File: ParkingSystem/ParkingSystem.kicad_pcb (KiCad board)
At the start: 2 copper layers, 55.9 x 61.5 mm, 43 parts, among them J1 PJ-002A, J2 0430450400, J3 Conn_ARM_JTAG_SWD_10, J4 Conn_01x04_Female, J5 0430450200, Q1 SSM3K333R,LF, Q2 SSM3K333R,LF, Q3 SSM3K333R,LF, Q4 SSM3K333R,LF, Q5 SSM3K333R,LF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

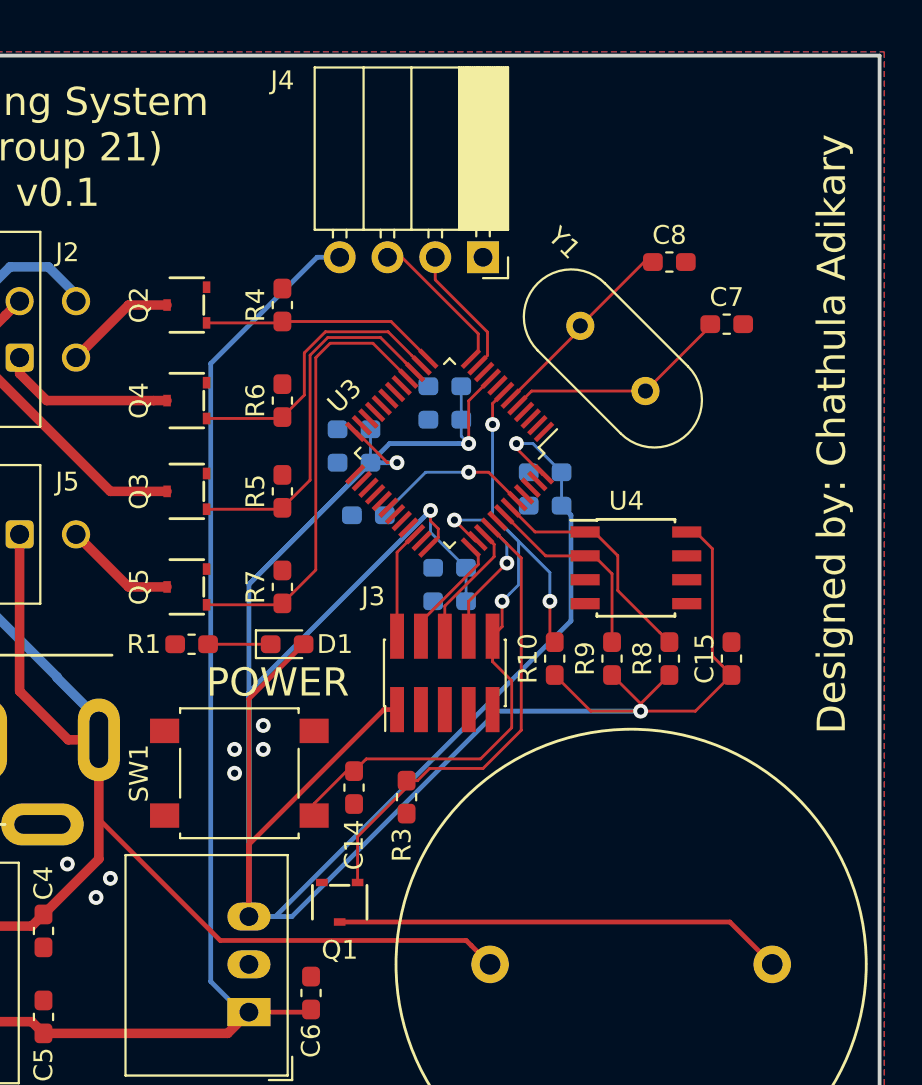
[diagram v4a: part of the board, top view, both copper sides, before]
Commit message: Add Ground Pours
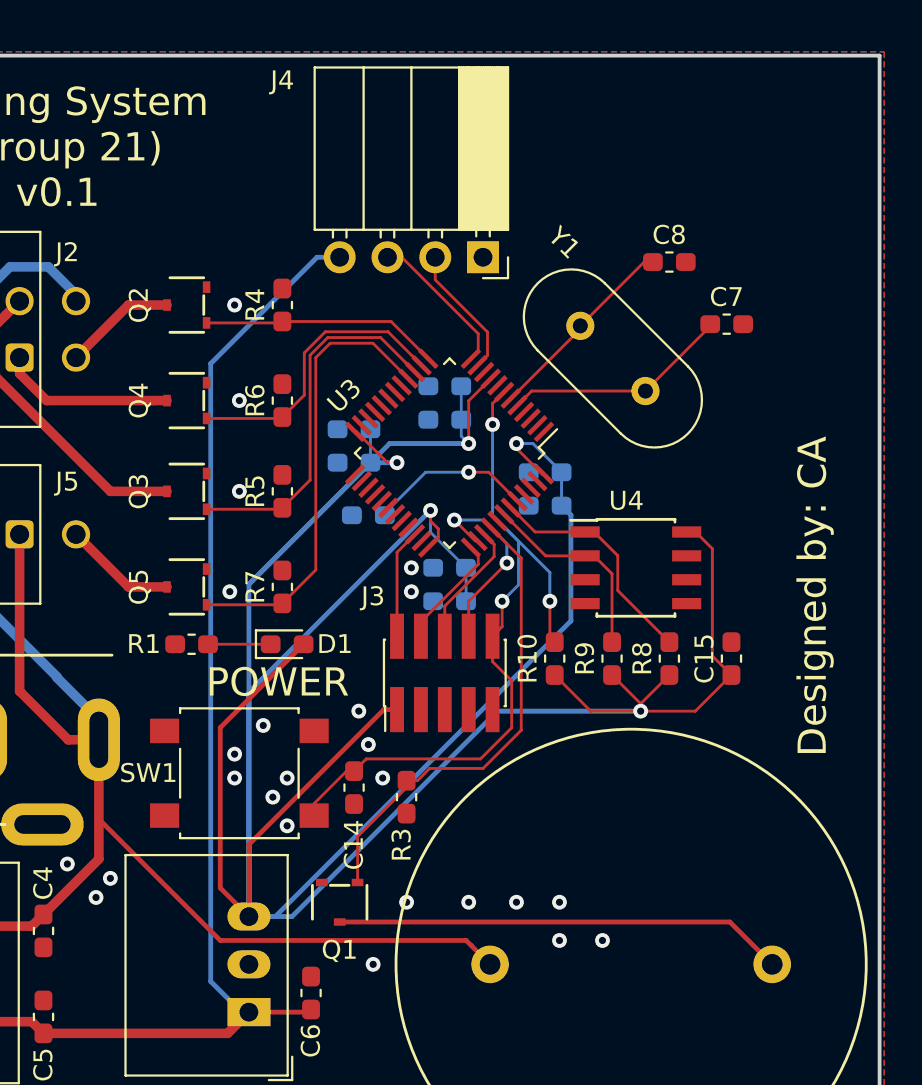
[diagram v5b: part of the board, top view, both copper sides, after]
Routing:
- net +3V3: track 205.7 -> 207.0 mm
- net GND: vias 7 -> 25
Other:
- board text added: "Designed by: CA"
- board text removed: "Designed by: Chathula Adikary"
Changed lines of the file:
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@@
     (thickness 1.6)
     (drawings 7)
-    (tracks 230)
+    (tracks 249)
     (zones 0)
     (modules 43)
@@
     (tags "capacitor handsolder")
     (attr smd)
-    (fp_text reference C2 (at 2.54 0 180) (layer B.SilkS)
+    (fp_text reference C2 (at 0 -1.524 180) (layer B.SilkS)
       (effects (font (size 1 1) (thickness 0.15)) (justify mirror))
     )
@@
     (tags "capacitor handsolder")
     (attr smd)
-    (fp_text reference C9 (at 2.54 0 180) (layer B.SilkS)
+    (fp_text reference C9 (at 0 1.27 180) (layer B.SilkS)
       (effects (font (size 1 1) (thickness 0.15)) (justify mirror))
     )
@@
     (tags "Tactile Switch")
     (attr smd)
-    (fp_text reference SW1 (at 5.334 0 270) (layer F.SilkS)
+    (fp_text reference SW1 (at 4.826 0) (layer F.SilkS)
       (effects (font (size 1 1) (thickness 0.15)))
     )
@@
     )
   )
-  (gr_text "Designed by: Chathula Adikary" (at 121.92 55.118 90) (layer F.SilkS)
+  (gr_text "Designed by: CA" (at 120.904 63.754 90) (layer F.SilkS)
     (effects (font (size 1.5 1.5) (thickness 0.3)))
   )
@@
     (effects (font (size 1.5 1.5) (thickness 0.3)))
   )
+  (via (at 99.568 62.23) (size 0.7874) (drill 0.381) (layers F.Cu B.Cu) (net 2))
+  (via (at 99.568 63.5) (size 0.7874) (drill 0.381) (layers F.Cu B.Cu) (net 2))
+  (via (at 97.282 71.628) (size 0.7874) (drill 0.381) (layers F.Cu B.Cu) (net 2))
   (via (at 106.934 64.008) (size 0.7874) (drill 0.381) (layers F.Cu B.Cu) (net 7))
   (via (at 102.616 57.15) (size 0.7874) (drill 0.381) (layers F.Cu B.Cu) (net 27))
@@
   (segment (start 90.932 76.941078) (end 98.105078 69.768) (width 0.254) (layer F.Cu) (net 1))
   (segment (start 90.932 80.772) (end 90.932 76.941078) (width 0.254) (layer F.Cu) (net 1))
-  (segment (start 90.932 69.201) (end 90.932 80.772) (width 0.254) (layer F.Cu) (net 1))
-  (segment (start 93.839 66.294) (end 90.932 69.201) (width 0.254) (layer F.Cu) (net 1))
   (segment (start 90.932 68.834) (end 100.584 59.182) (width 0.254) (layer B.Cu) (net 1))
   (segment (start 90.932 80.772) (end 90.932 68.834) (width 0.254) (layer B.Cu) (net 1))
@@
   (segment (start 114.667 69.85) (end 116.586 67.931) (width 0.1524) (layer F.Cu) (net 1))
   (segment (start 111.76 69.85) (end 114.667 69.85) (width 0.1524) (layer F.Cu) (net 1))
+  (segment (start 89.408 79.248) (end 90.932 80.772) (width 0.254) (layer F.Cu) (net 1))
+  (segment (start 93.839 66.294) (end 89.408 70.725) (width 0.254) (layer F.Cu) (net 1))
+  (segment (start 89.408 70.725) (end 89.408 79.248) (width 0.254) (layer F.Cu) (net 1))
   (via (at 82.804 79.756) (size 0.7874) (drill 0.381) (layers F.Cu B.Cu) (net 2))
   (via (at 83.566 78.74) (size 0.7874) (drill 0.381) (layers F.Cu B.Cu) (net 2))
   (via (at 81.28 77.978) (size 0.7874) (drill 0.381) (layers F.Cu B.Cu) (net 2))
   (via (at 91.694 70.612) (size 0.7874) (drill 0.381) (layers F.Cu B.Cu) (net 2))
-  (via (at 91.694 71.882) (size 0.7874) (drill 0.381) (layers F.Cu B.Cu) (net 2))
-  (via (at 90.17 71.882) (size 0.7874) (drill 0.381) (layers F.Cu B.Cu) (net 2))
-  (via (at 90.17 73.152) (size 0.7874) (drill 0.381) (layers F.Cu B.Cu) (net 2))
+  (via (at 92.202 74.422) (size 0.7874) (drill 0.381) (layers F.Cu B.Cu) (net 2))
+  (via (at 90.17 72.136) (size 0.7874) (drill 0.381) (layers F.Cu B.Cu) (net 2))
+  (via (at 92.964 75.946) (size 0.7874) (drill 0.381) (layers F.Cu B.Cu) (net 2))
+  (via (at 98.044 73.406) (size 0.7874) (drill 0.381) (layers F.Cu B.Cu) (net 2))
+  (via (at 90.17 48.26) (size 0.7874) (drill 0.381) (layers F.Cu B.Cu) (net 2))
+  (via (at 90.424 53.34) (size 0.7874) (drill 0.381) (layers F.Cu B.Cu) (net 2))
+  (via (at 90.424 58.166) (size 0.7874) (drill 0.381) (layers F.Cu B.Cu) (net 2))
+  (via (at 89.916 63.5) (size 0.7874) (drill 0.381) (layers F.Cu B.Cu) (net 2))
+  (via (at 92.964 73.406) (size 0.7874) (drill 0.381) (layers F.Cu B.Cu) (net 2))
+  (via (at 96.774 69.85) (size 0.7874) (drill 0.381) (layers F.Cu B.Cu) (net 2))
+  (via (at 90.17 73.406) (size 0.7874) (drill 0.381) (layers F.Cu B.Cu) (net 2))
+  (via (at 102.616 80.01) (size 0.7874) (drill 0.381) (layers F.Cu B.Cu) (net 2))
+  (via (at 105.156 80.01) (size 0.7874) (drill 0.381) (layers F.Cu B.Cu) (net 2))
+  (via (at 107.442 80.01) (size 0.7874) (drill 0.381) (layers F.Cu B.Cu) (net 2))
+  (via (at 107.442 82.042) (size 0.7874) (drill 0.381) (layers F.Cu B.Cu) (net 2))
+  (via (at 109.728 82.042) (size 0.7874) (drill 0.381) (layers F.Cu B.Cu) (net 2))
+  (via (at 99.314 80.01) (size 0.7874) (drill 0.381) (layers F.Cu B.Cu) (net 2))
+  (via (at 97.536 83.312) (size 0.7874) (drill 0.381) (layers F.Cu B.Cu) (net 2))
   (segment (start 81.326 71.374) (end 82.954 71.374) (width 0.508) (layer F.Cu) (net 3))
   (segment (start 78.74 68.788) (end 81.326 71.374) (width 0.508) (layer F.Cu) (net 3))
@@
     (connect_pads (clearance 0.1778))
     (min_thickness 0.1778)
-    (fill yes (arc_segments 16) (thermal_gap 0.508) (thermal_bridge_width 0.508))
+    (fill (arc_segments 16) (thermal_gap 0.508) (thermal_bridge_width 0.508))
     (polygon
       (pts
@@
     (connect_pads (clearance 0.1778))
     (min_thickness 0.1778)
-    (fill yes (arc_segments 16) (thermal_gap 0.508) (thermal_bridge_width 0.508))
+    (fill (arc_segments 16) (thermal_gap 0.508) (thermal_bridge_width 0.508))
     (polygon
       (pts

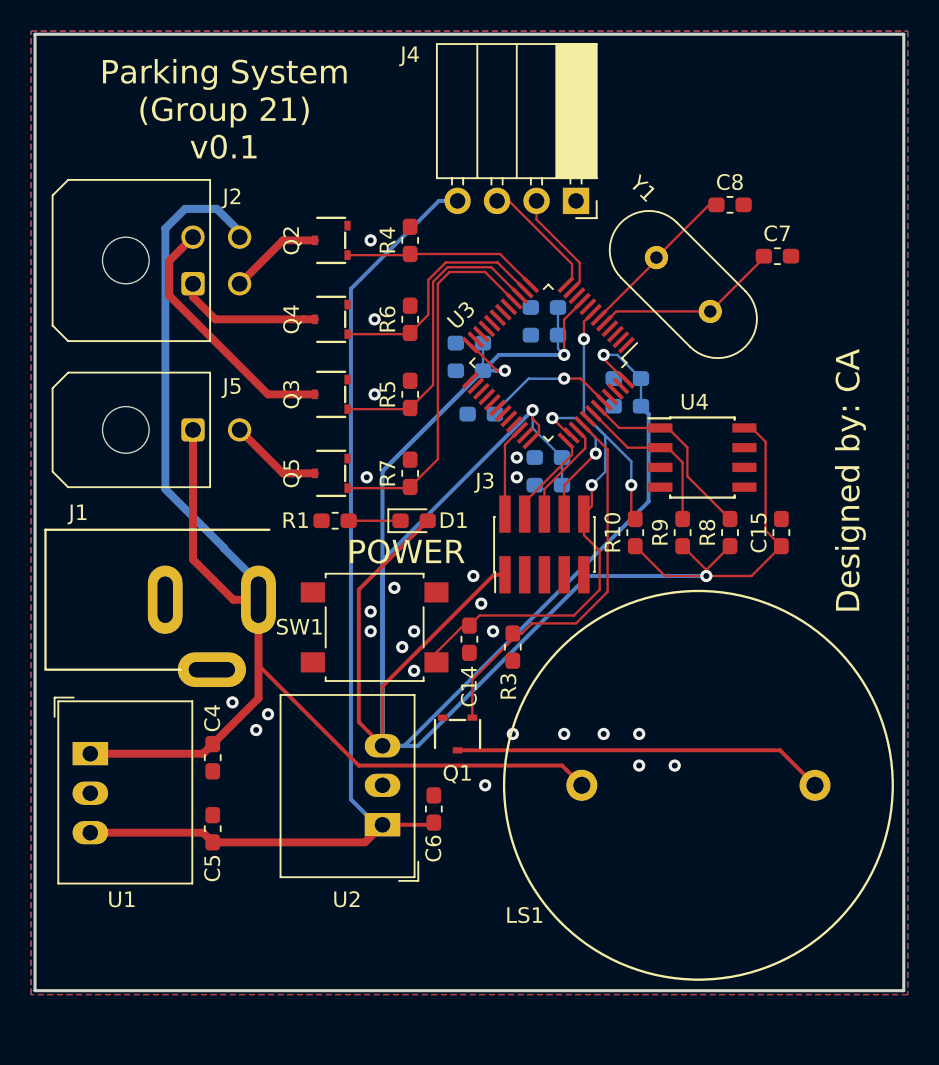
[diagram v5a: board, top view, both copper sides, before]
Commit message: Add Mounting Holes
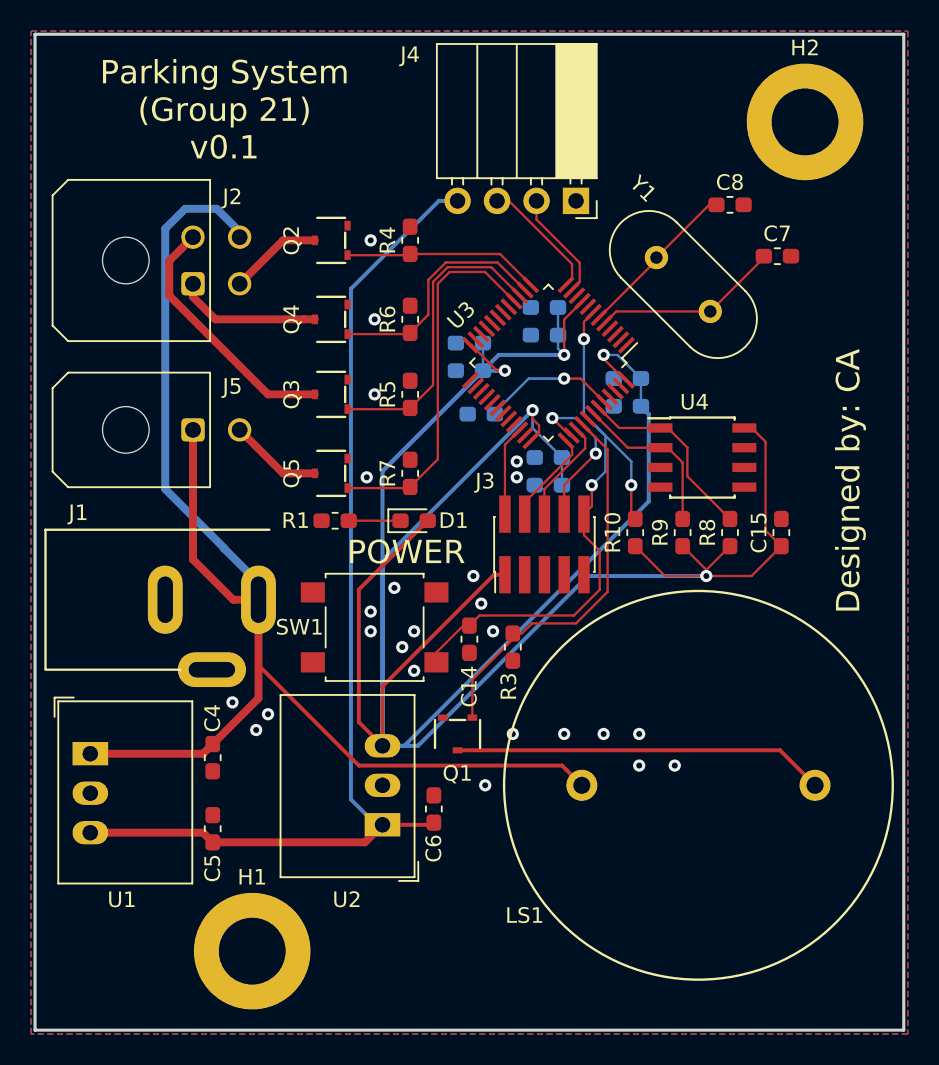
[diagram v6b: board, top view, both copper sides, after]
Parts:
- added H1: MountingHole, MountingHole:MountingHole_4.3mm_M4_DIN965_Pad, F.Cu at (82.5, 94.0)
- added H2: MountingHole, MountingHole:MountingHole_4.3mm_M4_DIN965_Pad, F.Cu at (118.1, 40.6)
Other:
- board size 55.9 x 61.5 mm -> 55.9 x 64.1 mm
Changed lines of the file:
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@@
-(kicad_pcb (version 20171130) (host pcbnew "(5.0.2)-1")
+(kicad_pcb (version 20171130) (host pcbnew 5.0.2-bee76a0~70~ubuntu18.04.1)
   (general
     (thickness 1.6)
@@
     (tracks 249)
     (zones 0)
-    (modules 43)
+    (modules 45)
     (nets 54)
   )
@@
   )
   (setup
-    (last_trace_width 0.1524)
+    (last_trace_width 0.254)
     (user_trace_width 0.1524)
     (user_trace_width 0.508)
@@
     (add_net "Net-(U4-Pad3)")
   )
+  (module MountingHole:MountingHole_4.3mm_M4_DIN965_Pad (layer F.Cu)
+    (at 118.11 40.64)
+    (descr "Mounting Hole 4.3mm, M4, DIN965")
+    (tags "mounting hole 4.3mm m4 din965")
+    (attr virtual)
+    (fp_text reference H2 (at 0 -4.75) (layer F.SilkS)
+      (effects (font (size 1 1) (thickness 0.15)))
+    )
+    (fp_text value MountingHole (at 0 4.75) (layer F.Fab)
+      (effects (font (size 1 1) (thickness 0.15)))
+    )
+    (fp_circle (center 0 0) (end 4 0) (layer F.CrtYd) (width 0.05))
+    (fp_circle (center 0 0) (end 3.75 0) (layer Cmts.User) (width 0.15))
+    (fp_text user %R (at 0.3 0) (layer F.Fab)
+      (effects (font (size 1 1) (thickness 0.15)))
+    )
+    (pad 1 thru_hole circle (at 0 0) (size 7.5 7.5) (drill 4.3) (layers *.Cu *.Mask))
+  )
+  (module MountingHole:MountingHole_4.3mm_M4_DIN965_Pad (layer F.Cu)
+    (at 82.55 93.98)
+    (descr "Mounting Hole 4.3mm, M4, DIN965")
+    (tags "mounting hole 4.3mm m4 din965")
+    (attr virtual)
+    (fp_text reference H1 (at 0 -4.75) (layer F.SilkS)
+      (effects (font (size 1 1) (thickness 0.15)))
+    )
+    (fp_text value MountingHole (at 0 4.75) (layer F.Fab)
+      (effects (font (size 1 1) (thickness 0.15)))
+    )
+    (fp_text user %R (at 0.3 0) (layer F.Fab)
+      (effects (font (size 1 1) (thickness 0.15)))
+    )
+    (fp_circle (center 0 0) (end 3.75 0) (layer Cmts.User) (width 0.15))
+    (fp_circle (center 0 0) (end 4 0) (layer F.CrtYd) (width 0.05))
+    (pad 1 thru_hole circle (at 0 0) (size 7.5 7.5) (drill 4.3) (layers *.Cu *.Mask))
+  )
   (module Converter_DCDC:Converter_DCDC_RECOM_R-78E-0.5_THT (layer F.Cu)
     (at 72.136 81.28 270)
@@
     (effects (font (size 1.5 1.5) (thickness 0.3)))
   )
-  (gr_line (start 124.46 96.52) (end 68.58 96.52) (layer Edge.Cuts) (width 0.2))
-  (gr_line (start 124.46 35) (end 124.46 96.52) (layer Edge.Cuts) (width 0.2))
+  (gr_line (start 124.46 99.06) (end 68.58 99.06) (layer Edge.Cuts) (width 0.2))
+  (gr_line (start 124.46 35) (end 124.46 99.06) (layer Edge.Cuts) (width 0.2))
   (gr_line (start 68.58 35) (end 124.46 35) (layer Edge.Cuts) (width 0.2))
-  (gr_line (start 68.58 96.52) (end 68.58 35) (layer Edge.Cuts) (width 0.2))
+  (gr_line (start 68.58 99.06) (end 68.58 35) (layer Edge.Cuts) (width 0.2))
   (gr_text POWER (at 92.456 68.326) (layer F.SilkS)
     (effects (font (size 1.5 1.5) (thickness 0.3)))
   )
-  (via (at 99.568 62.23) (size 0.7874) (drill 0.381) (layers F.Cu B.Cu) (net 2))
-  (via (at 99.568 63.5) (size 0.7874) (drill 0.381) (layers F.Cu B.Cu) (net 2))
-  (via (at 97.282 71.628) (size 0.7874) (drill 0.381) (layers F.Cu B.Cu) (net 2))
-  (via (at 106.934 64.008) (size 0.7874) (drill 0.381) (layers F.Cu B.Cu) (net 7))
-  (via (at 102.616 57.15) (size 0.7874) (drill 0.381) (layers F.Cu B.Cu) (net 27))
   (via (at 111.76 69.85) (size 0.7874) (drill 0.381) (layers F.Cu B.Cu) (net 1))
-  (via (at 101.854 59.69) (size 0.7874) (drill 0.381) (layers F.Cu B.Cu) (net 17))
   (via (at 100.584 59.182) (size 0.7874) (drill 0.381) (layers F.Cu B.Cu) (net 1))
   (via (at 98.806 56.642) (size 0.7874) (drill 0.381) (layers F.Cu B.Cu) (net 1))
-  (via (at 104.394 64.008) (size 0.7874) (drill 0.381) (layers F.Cu B.Cu) (net 7))
   (via (at 102.616 55.626) (size 0.7874) (drill 0.381) (layers F.Cu B.Cu) (net 1))
   (segment (start 97.395 56.642) (end 97.395 54.864) (width 0.1524) (layer B.Cu) (net 1))
@@
   (segment (start 93.839 66.294) (end 89.408 70.725) (width 0.254) (layer F.Cu) (net 1))
   (segment (start 89.408 70.725) (end 89.408 79.248) (width 0.254) (layer F.Cu) (net 1))
+  (via (at 99.568 62.484) (size 0.7874) (drill 0.381) (layers F.Cu B.Cu) (net 2))
+  (via (at 99.568 63.5) (size 0.7874) (drill 0.381) (layers F.Cu B.Cu) (net 2))
+  (via (at 97.282 71.628) (size 0.7874) (drill 0.381) (layers F.Cu B.Cu) (net 2))
   (via (at 82.804 79.756) (size 0.7874) (drill 0.381) (layers F.Cu B.Cu) (net 2))
   (via (at 83.566 78.74) (size 0.7874) (drill 0.381) (layers F.Cu B.Cu) (net 2))
@@
   (segment (start 111.942354 45.974) (end 112.409 45.974) (width 0.1524) (layer F.Cu) (net 6))
   (segment (start 108.549177 49.367177) (end 111.942354 45.974) (width 0.1524) (layer F.Cu) (net 6))
+  (via (at 106.934 64.008) (size 0.7874) (drill 0.381) (layers F.Cu B.Cu) (net 7))
+  (via (at 104.394 64.008) (size 0.7874) (drill 0.381) (layers F.Cu B.Cu) (net 7))
   (segment (start 96.125 73.039) (end 96.52 73.039) (width 0.1524) (layer F.Cu) (net 7))
   (segment (start 94.399 75.402) (end 94.399 74.765) (width 0.1524) (layer F.Cu) (net 7))
@@
   (segment (start 101.346 65.868) (end 101.346 64.262) (width 0.1524) (layer F.Cu) (net 15))
   (segment (start 101.346 64.262) (end 103.968807 61.639193) (width 0.1524) (layer F.Cu) (net 15))
+  (via (at 101.854 59.69) (size 0.7874) (drill 0.381) (layers F.Cu B.Cu) (net 17))
   (segment (start 102.616 64.008) (end 102.616 65.868) (width 0.1524) (layer F.Cu) (net 17))
   (via (at 104.648 61.976) (size 0.7874) (drill 0.381) (layers F.Cu B.Cu) (net 17))
@@
   (segment (start 92.635 64.196) (end 92.71 64.121) (width 0.1524) (layer F.Cu) (net 26))
   (segment (start 88.68 64.196) (end 92.635 64.196) (width 0.1524) (layer F.Cu) (net 26))
+  (via (at 102.616 57.15) (size 0.7874) (drill 0.381) (layers F.Cu B.Cu) (net 27))
   (segment (start 103.676661 57.15) (end 105.206245 58.679584) (width 0.1524) (layer F.Cu) (net 27))
   (segment (start 102.616 57.15) (end 103.676661 57.15) (width 0.1524) (layer F.Cu) (net 27))
@@
   (zone (net 2) (net_name GND) (layer F.Cu) (hatch edge 0.508)
     (connect_pads (clearance 0.1778))
-    (min_thickness 0.1778)
-    (fill (arc_segments 16) (thermal_gap 0.508) (thermal_bridge_width 0.508))
+    (min_thickness 0.254)
+    (fill yes (arc_segments 16) (thermal_gap 0.508) (thermal_bridge_width 0.508))
     (polygon
       (pts
-        (xy 68.326 96.774) (xy 68.326 34.798) (xy 124.714 34.798) (xy 124.714 96.774)
+        (xy 68.326 99.314) (xy 68.326 34.798) (xy 124.714 34.798) (xy 124.714 99.314)
       )
     )
@@
   (zone (net 2) (net_name GND) (layer B.Cu) (hatch edge 0.508)
     (connect_pads (clearance 0.1778))
-    (min_thickness 0.1778)
-    (fill (arc_segments 16) (thermal_gap 0.508) (thermal_bridge_width 0.508))
+    (min_thickness 0.254)
+    (fill yes (arc_segments 16) (thermal_gap 0.508) (thermal_bridge_width 0.508))
     (polygon
       (pts
-        (xy 68.326 96.774) (xy 68.326 34.798) (xy 124.714 34.798) (xy 124.714 96.774)
+        (xy 68.326 99.314) (xy 68.326 34.798) (xy 124.714 34.798) (xy 124.714 99.314)
       )
     )
